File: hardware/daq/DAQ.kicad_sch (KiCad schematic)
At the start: 169 parts, among them J1 ICD15S13E4GX00LF, J2 ICD15S13E4GX00LF, J3 ICD15S13E4GX00LF, J4 ICD26S13E4GX00LF, P1 0022272021, U1 ADS124S08IRHBT, U2 ADS124S08IRHBT, U3 LT6654BMPS6-5-TRMPBF, U4 LM1086IS-5.0_NOPB, U5 TPS73801DCQR, U6 TPSM63603RDHR, U7 TPSM63603RDHR, U8 TPSM63603RDHR, U9 ADS124S08IRHBT

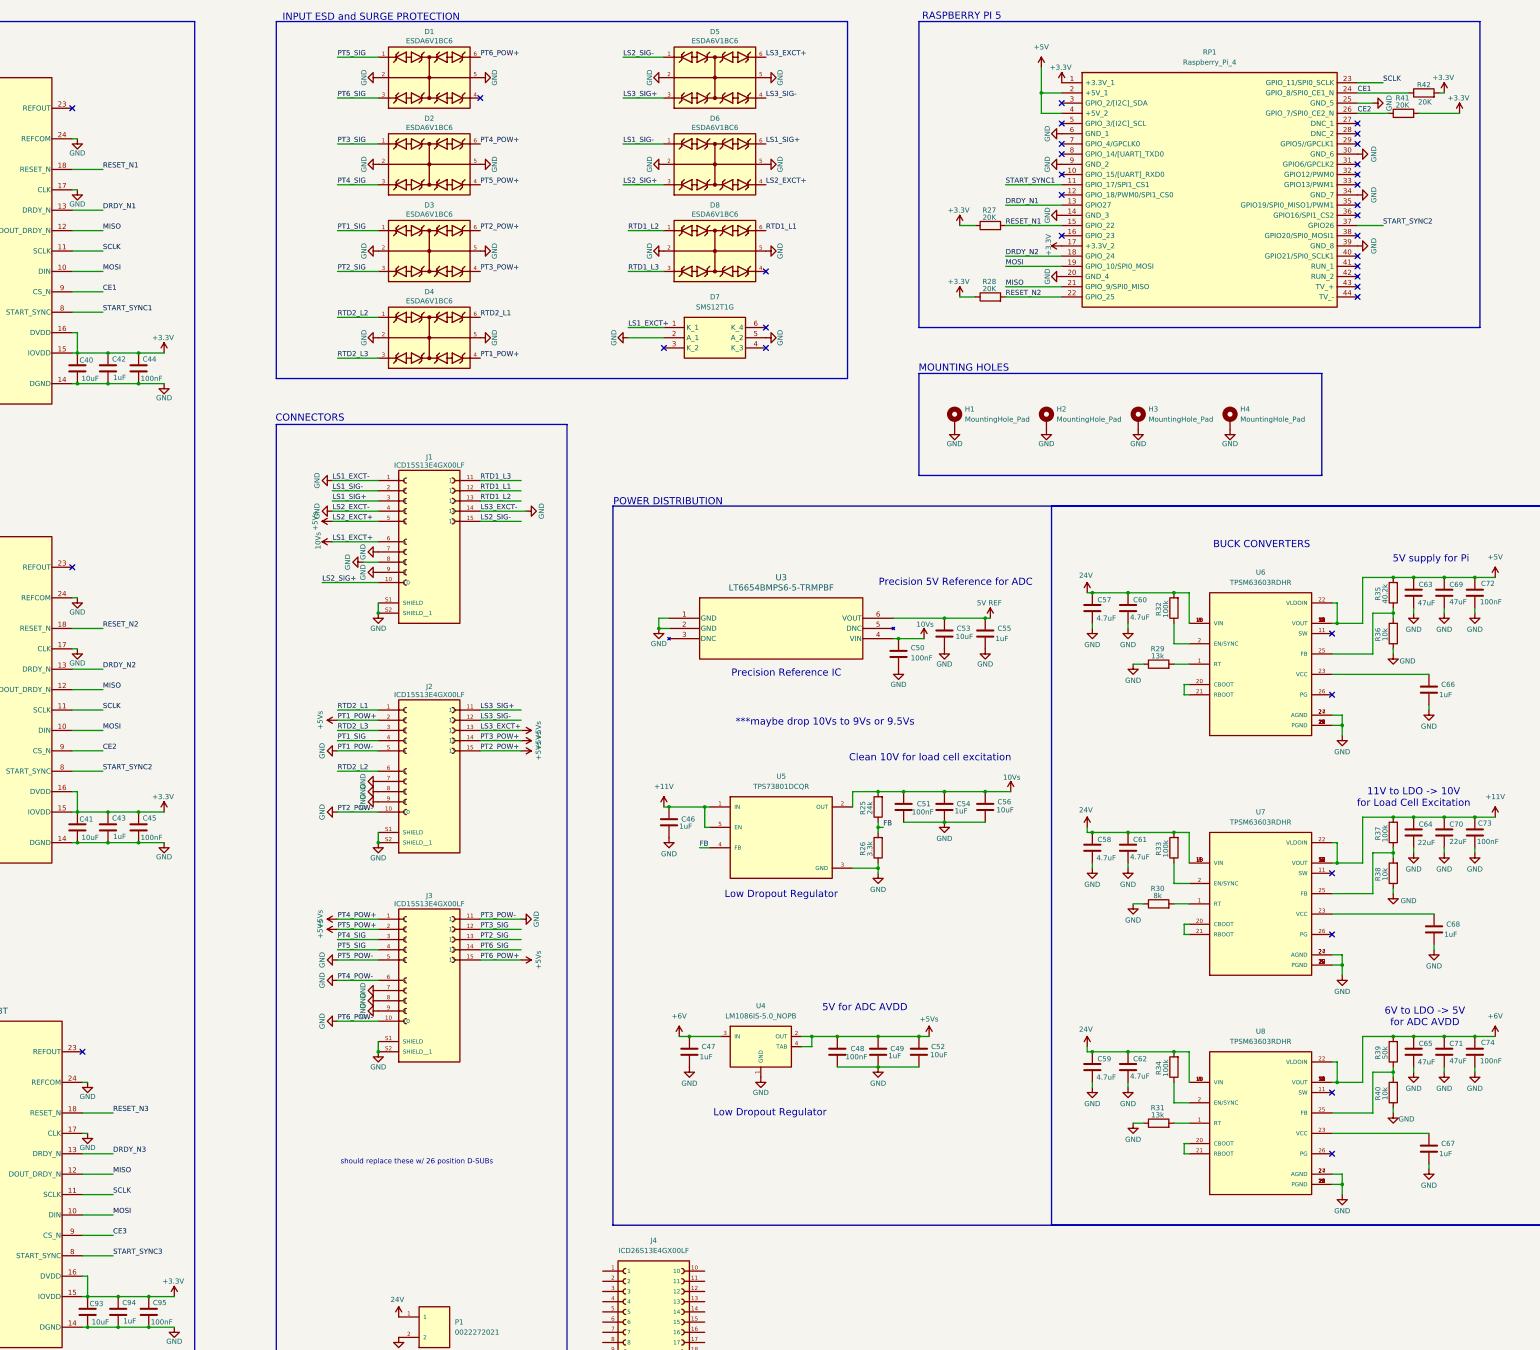
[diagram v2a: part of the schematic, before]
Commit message: Allocated Pi GPIO to valves
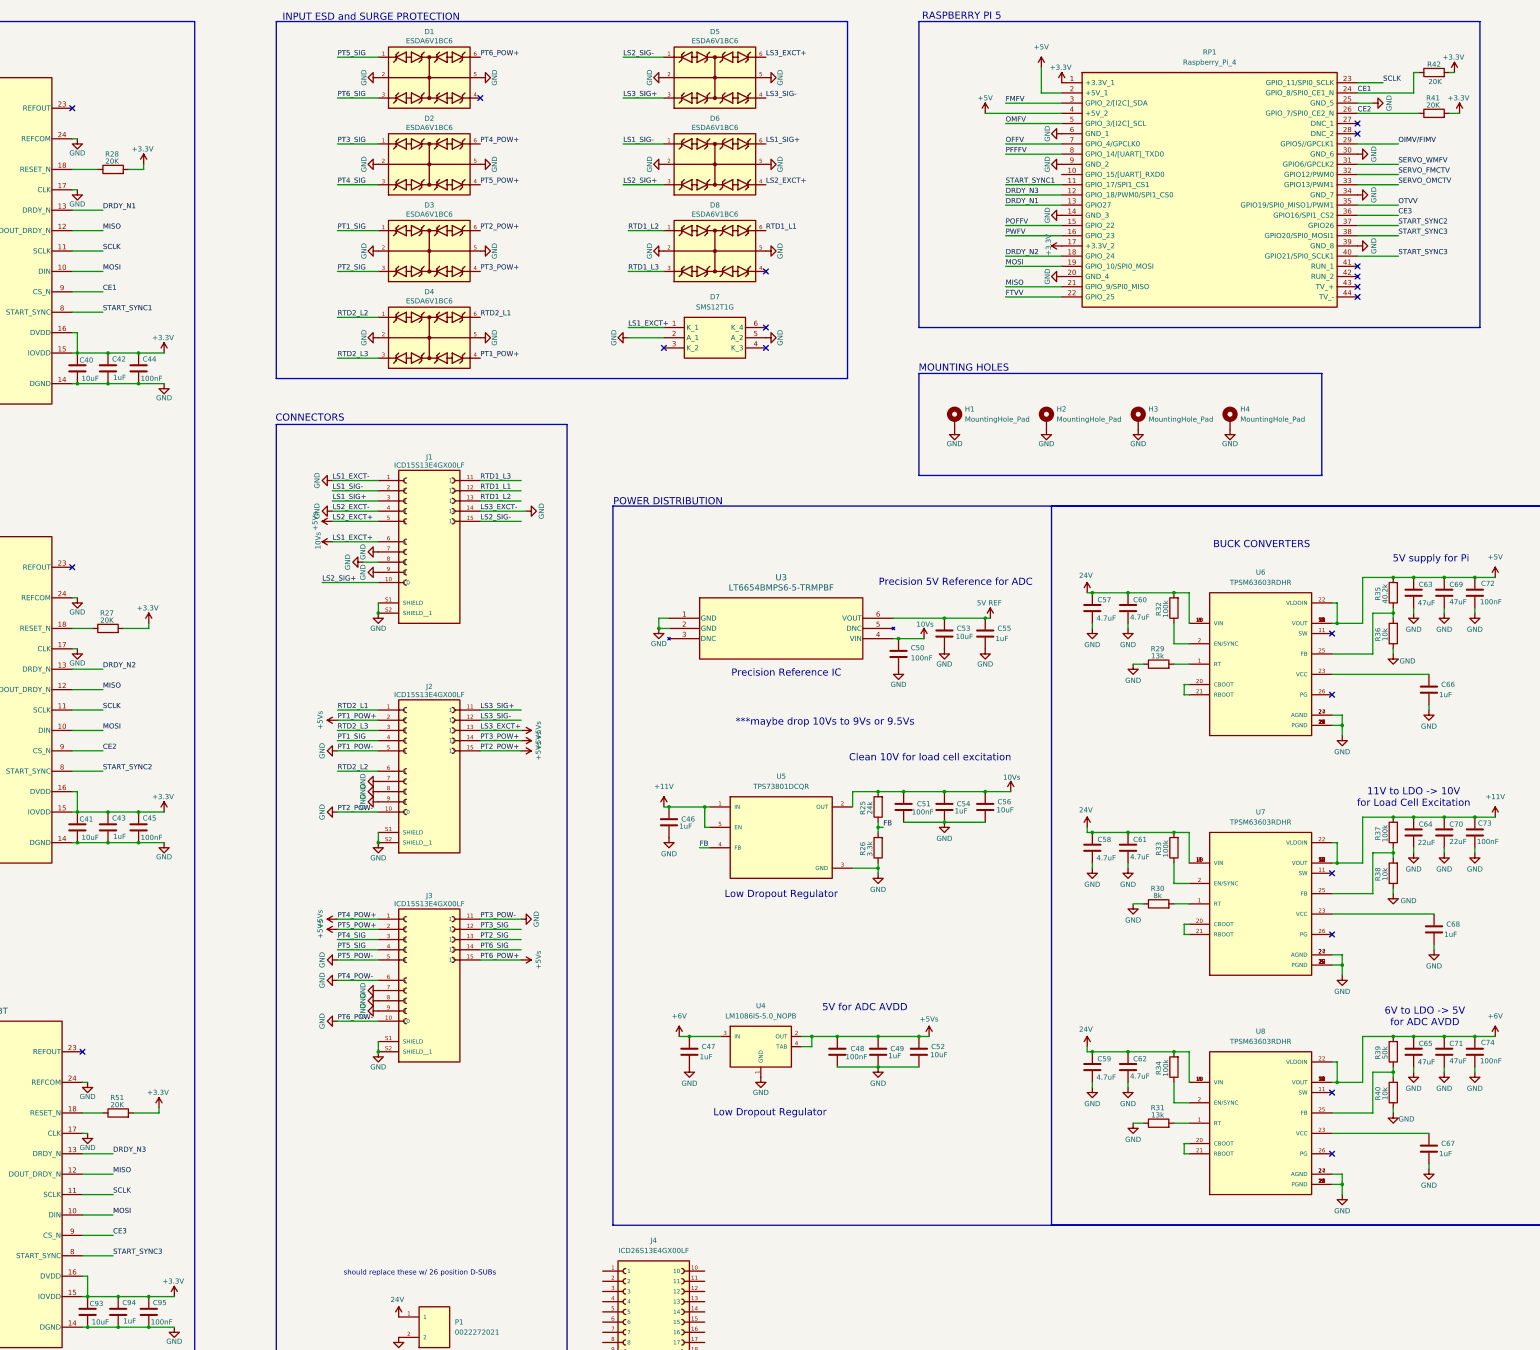
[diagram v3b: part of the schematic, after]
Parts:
- added R51: 20K, CRCW060320K0FKEA:RESC1508X50N, symbol Device:R
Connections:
- net +3.3V: now also R27.2, R28.2, R51.2; no longer R27.1, R28.1
- net CE3: now also RP1.36 (GPIO16/SPI1_CS2)
- net DRDY_N3: now also RP1.12 (GPIO_18/PWM0/SPI1_CS0)
- net START_SYNC3: now also RP1.38 (GPIO20/SPI0_MOSI1), RP1.40 (GPIO21/SPI0_SCLK1)
- net PWFV: now reaches RP1.16 (GPIO_23)
- net OIMV/FIMV: now reaches RP1.29 (GPIO5//GPCLK1)
- net FMFV: now reaches RP1.3 (GPIO_2/[I2C]_SDA)
- net SERVO_WMFV: now reaches RP1.31 (GPIO6/GPCLK2)
- net SERVO_FMCTV: now reaches RP1.32 (GPIO12/PWM0)
- net SERVO_OMCTV: now reaches RP1.33 (GPIO13/PWM1)
- net OTVV: now reaches RP1.35 (GPIO19/SPI0_MISO1/PWM1)
- net OMFV: now reaches RP1.5 (GPIO_3/[I2C]_SCL)
- net OFFV: now reaches RP1.7 (GPIO_4/GPCLK0)
- net PFFFV: now reaches RP1.8 (GPIO_14/[UART]_TXD0)
- removed net RESET_N1: R27.2, RP1.15 (GPIO_22), U1.18 (RESET_N)
- removed net RESET_N2: R28.2, RP1.22 (GPIO_25), U2.18 (RESET_N)
- net RESET_N3: no longer names the net of U9.18 (RESET_N)
- net RESET_N3: now also R51.1
- new net: R28.1, U1.18 (RESET_N)
- new net: R27.1, U2.18 (RESET_N)
- new net FTVV: RP1.22 (GPIO_25)
- new net POFFV: RP1.15 (GPIO_22)
- no-connect marks 38 -> 23
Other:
- moved on the sheet: R27, R41, R42

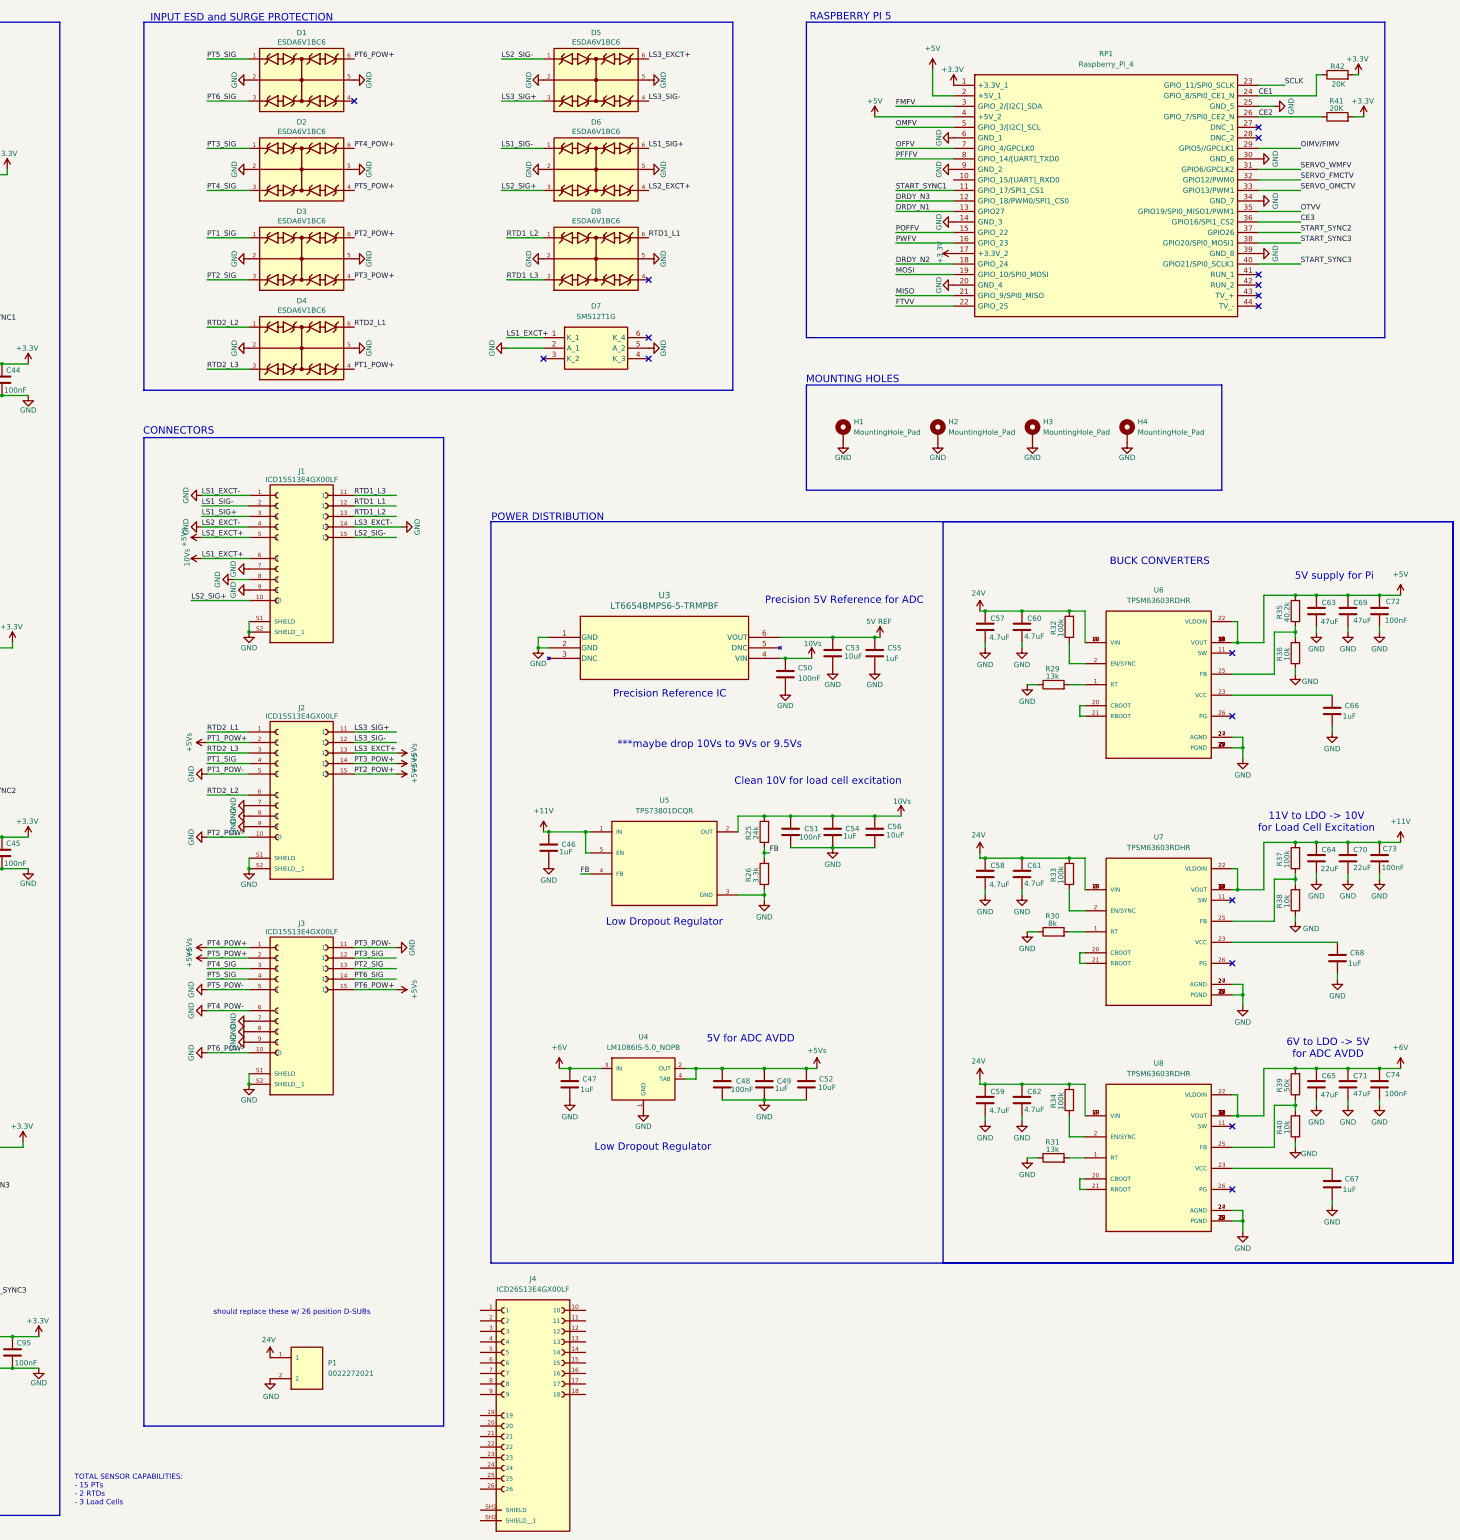
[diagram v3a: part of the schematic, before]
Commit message: added SH74AHCT125 to schem for uart comms with servo
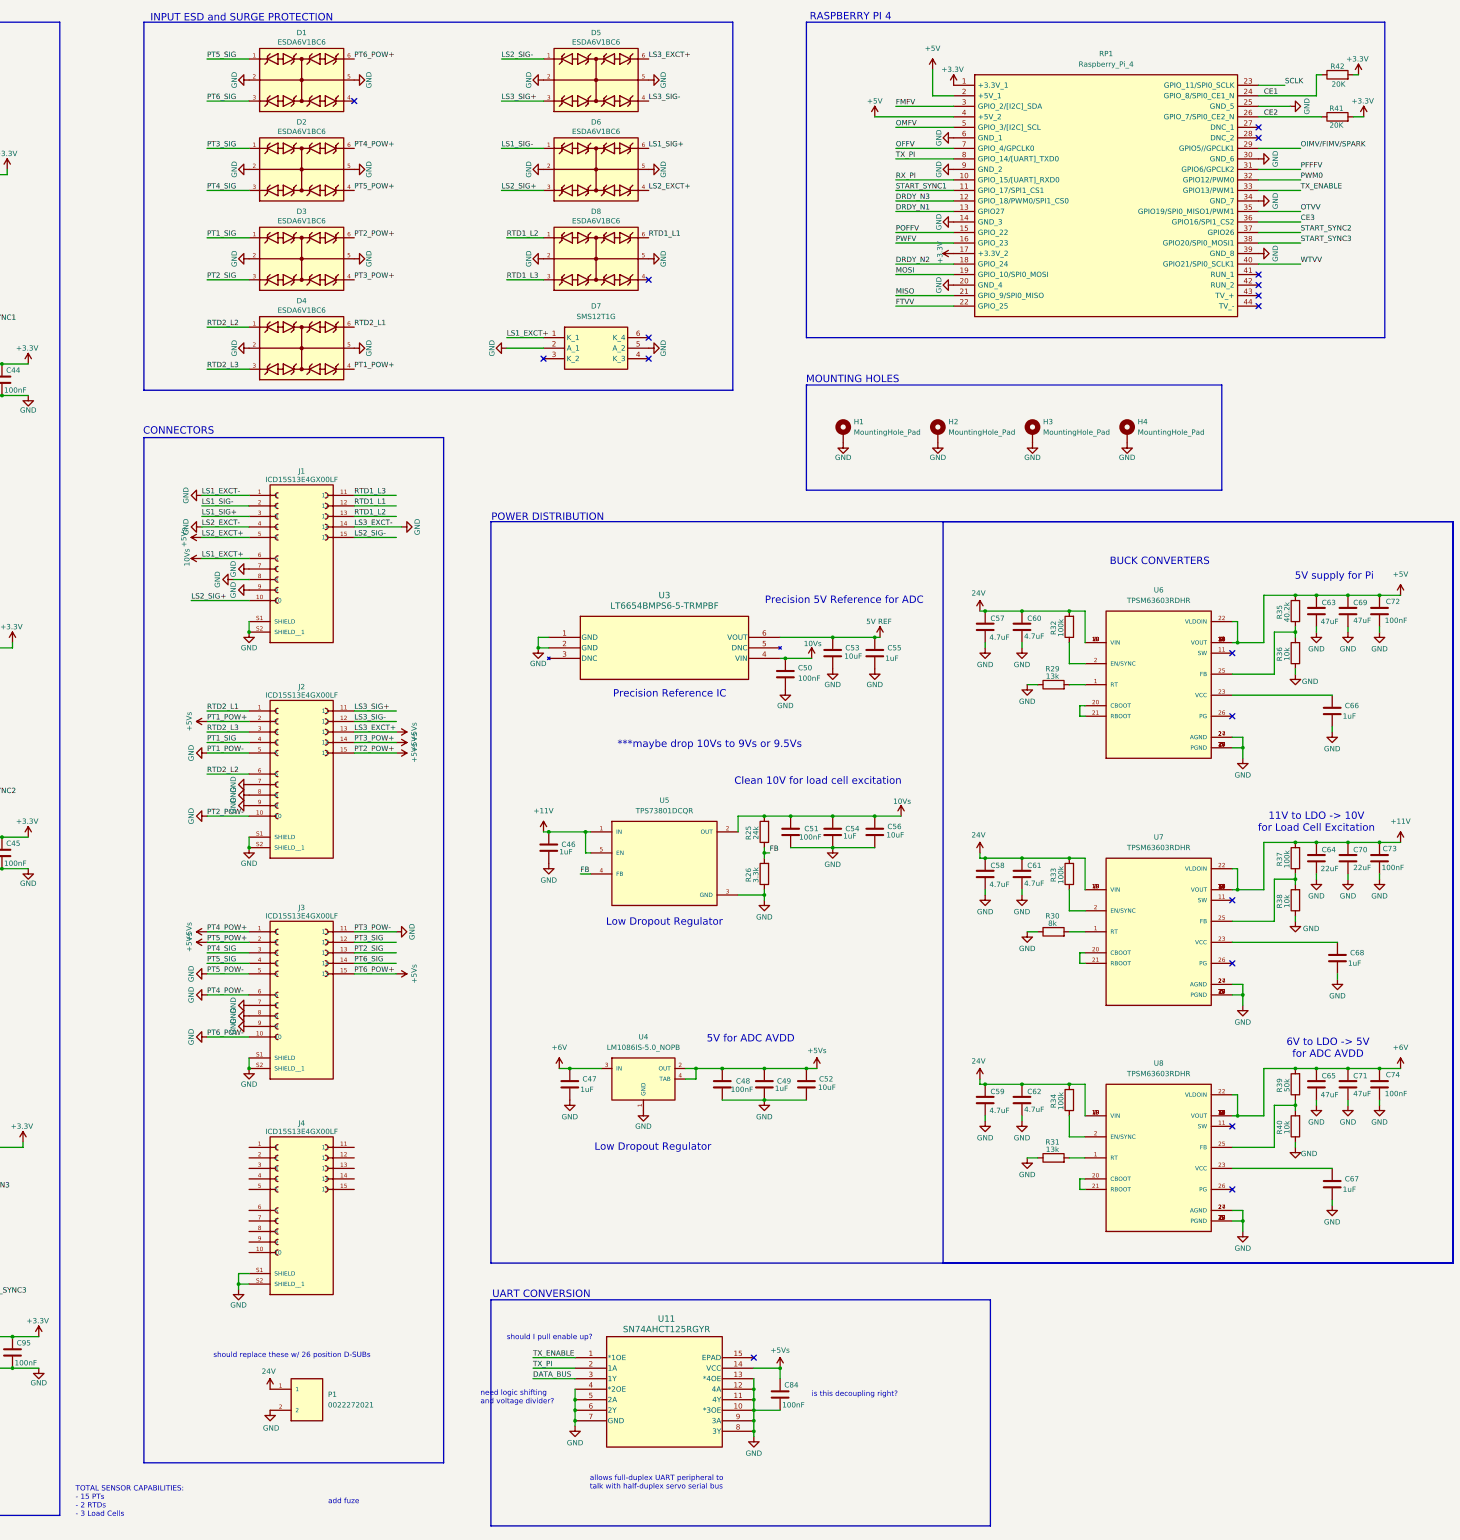
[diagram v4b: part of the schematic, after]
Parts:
- removed J4: ICD26S13E4GX00LF, ICD26S13E4GX00LF:AMPHENOL_ICD26S13E4GX00LF, symbol Connector:ICD26S13E4GX00LF
- added C84: 100nF, VJ0603Y104JXXAC:CAPC1608X97N, symbol Device:C
- added J4: ICD15S13E4GX00LF, ICD15S13:AMPHENOL_ICD15S13E4GX00LF, symbol ICD15S13E4GX00LF:ICD15S13E4GX00LF
- added U11: SN74AHCT125RGYR, RGY14_2P05X2P05, symbol SN74AHCT125:SN74AHCT125RGYR
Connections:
- net SERVO_WMFV is gone; now on net PFFFV: RP1.31 (GPIO6/GPCLK2)
- net +5Vs: now also C84.1, U11.14 (VCC)
- net GND: now also C84.2, J4.S1 (SHIELD), J4.S2 (SHIELD__1), U11.10 (*3OE), U11.11 (4Y), U11.12 (4A), U11.13 (*4OE), U11.4 (*2OE), U11.5 (2A), U11.6 (2Y), U11.7 (GND), U11.8 (3Y), U11.9 (3A)
- net PFFFV: no longer RP1.8 (GPIO_14/[UART]_TXD0)
- net START_SYNC3: no longer RP1.40 (GPIO21/SPI0_SCLK1)
- net RX_PI: now reaches RP1.10 (GPIO_15/[UART]_RXD0)
- net OIMV/FIMV renamed OIMV/FIMV/SPARK
- net SERVO_FMCTV renamed PWM0
- net SERVO_OMCTV renamed TX_ENABLE
- net TX_ENABLE: now also U11.1 (*1OE)
- new net DATA_BUS: U11.3 (1Y)
- new net TX_PI: RP1.8 (GPIO_14/[UART]_TXD0), U11.2 (1A)
- new net WTVV: RP1.40 (GPIO21/SPI0_SCLK1)
- no-connect marks 23 -> 24
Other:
- note added: "RASPBERRY PI 4"
- note added: "UART CONVERSION"
- note added: "add fuze"
- note added: "allows full-duplex UART peripheral to talk with half-duplex servo serial bus"
- note added: "is this decoupling right?"
- note added: "need logic shifting and voltage divider?"
- note added: "should I pull enable up?"
- note removed: "RASPBERRY PI 5"
- moved on the sheet: J2, J3, P1

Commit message: FIXED ALL OF THE STUPID FOOTPRINT ISSUES
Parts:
- added R52: 1K, CRCW060320K0FKEA:RESC1508X50N, symbol Device:R
- added R53: 2.2K, CRCW060320K0FKEA:RESC1508X50N, symbol Device:R
- added R54: 20K, CRCW060320K0FKEA:RESC1508X50N, symbol Device:R
- R1, R10, R11, R12, R13, R14, R15, R16, R17, R18, R19, R2, R20, R21, R22, R23, R24, R3, R4, R43, R44, R45, R46, R47, R48, R49, R5, R50, R6, R7, R8, R9: footprint footprints10kR:RC0603N_YAG-M -> Resistor_SMD:R_0603_1608Metric
- U11: footprint RGY14_2P05X2P05 -> ul_SN74AHCT125RGYR:RGY14_2P05X2P05
- U2, U9: footprint footprintsADC:RHB0032M -> ADS124S08IRHBT:QFN50P500X500X100-33N
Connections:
- net +3.3V: now also R54.1
- net +5Vs: now also U11.10 (*3OE), U11.12 (4A), U11.13 (*4OE), U11.9 (3A)
- net DATA_BUS: now also R52.2
- net GND: now also R53.2; no longer U11.10 (*3OE), U11.11 (4Y), U11.12 (4A), U11.13 (*4OE), U11.6 (2Y), U11.8 (3Y), U11.9 (3A)
- net RX_PI: now also R52.1, R53.1
- net TX_ENABLE: now also R54.2
- net PWM0: no longer names the net of RP1.32 (GPIO12/PWM0)
- no-connect marks 24 -> 28
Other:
- note added: "This IC allows the Pi's full-duplex UART peripheral to talk with the half-duplex servo serial bus"
- note added: "Voltage divider to step the 5V signal from the servo serial bus to a tolerable GPIO voltage (~3.44V)"
- note removed: "allows full-duplex UART peripheral to talk with half-duplex servo serial bus"
- note removed: "is this decoupling right?"
- note removed: "need logic shifting and voltage divider?"
- note removed: "should I pull enable up?"
- title: Data Acquisition Board -> DAQ + F3C
- moved on the sheet: C25, C84, U11
